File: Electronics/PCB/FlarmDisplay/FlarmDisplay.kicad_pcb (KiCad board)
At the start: 2 copper layers, 43 x 25 mm, 65 parts, among them J1 RJ12, J2 SWD, SW1 RESET, SW2 BOOT, U1 IPN80R3K3P7ATMA1, U2 STM32F334K8Ux, U3 TLC5928, U4 TLC5928, Y1 16MHz

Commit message: Latest
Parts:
- C1, C10, C11, C14, C2, C3, C4, C5, C6, C7, C8, C9, R4, U2, U4, Y1: moved to B.Cu
- J1: footprint Connector_RJ:RJ12_Amphenol_54601 -> FlarmDisplay:RJE231660413T; moved to B.Cu
- U1: footprint Package_TO_SOT_SMD:SOT-323_SC-70 -> Package_TO_SOT_SMD:SOT-223-3_TabPin2; moved to B.Cu
- moved J1 95.1 mm to (101.5, 122.5), turned to 270 degrees
- moved C12 31.3 mm to (95.8, 134.1), turned to 180 degrees
- moved R3 20.1 mm to (88.0, 129.9), turned to 270 degrees
- moved R4 19.8 mm to (82.3, 122.0), turned to 270 degrees
- moved C14 19.7 mm to (81.9, 118.3), turned to 270 degrees
- moved R2 18.5 mm to (120.7, 113.3), turned to 90 degrees
- moved SW2 14.3 mm to (115.1, 113.4), turned to 90 degrees
- moved R1 14.0 mm to (97.7, 118.2), turned to 90 degrees
- moved C7 14.0 mm to (119.9, 123.7), turned to 270 degrees
- moved U4 12.8 mm to (85.9, 117.6)
- moved C6 12.5 mm to (118.9, 123.7)
- moved C11 10.3 mm to (116.7, 130.0)
- moved U1 9.16 mm to (87.5, 130.7), turned to 0 degrees
- moved C9 8.99 mm to (110.9, 115.4), turned to 90 degrees
- moved C10 8.20 mm to (114.1, 130.0), turned to 0 degrees
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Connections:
- net ERR_READ renamed Net-(U4-Pad19)
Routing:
- net +3V3: track 0.00 -> 161.2 mm, vias 0 -> 19
- net GND: track 0.00 -> 128.0 mm, vias 0 -> 15
- net Net-(U2-Pad13): track 0.00 -> 50.0 mm, vias 0 -> 3
- net Net-(U2-Pad12): track 0.00 -> 46.6 mm, vias 0 -> 3
- net Net-(TP3-Pad1): track 0.00 -> 35.8 mm, vias 0 -> 3
- net Net-(D3-Pad1): track 0.00 -> 35.3 mm, vias 0 -> 2
- net Net-(TP4-Pad1): track 0.00 -> 35.0 mm, vias 0 -> 3
- net Net-(U2-Pad14): track 0.00 -> 32.7 mm, vias 0 -> 2
- net Net-(BZ1-Pad2): track 0.00 -> 30.8 mm, vias 0 -> 2
- net NRST: track 0.00 -> 30.0 mm, vias 0 -> 1
- net Net-(D6-Pad1): track 0.00 -> 28.3 mm, vias 0 -> 2
- net Net-(D5-Pad1): track 0.00 -> 26.7 mm, vias 0 -> 2
- net Net-(U2-Pad11): track 0.00 -> 26.3 mm, vias 0 -> 2
- net Net-(U3-Pad19): track 0.00 -> 26.1 mm, vias 0 -> 2
- net SWDAT: track 0.00 -> 25.2 mm, vias 0 -> 2
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- added copper zone on In1.Cu, net +3V3
- added copper zone on In2.Cu, net GND
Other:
- copper layers 2 -> 4

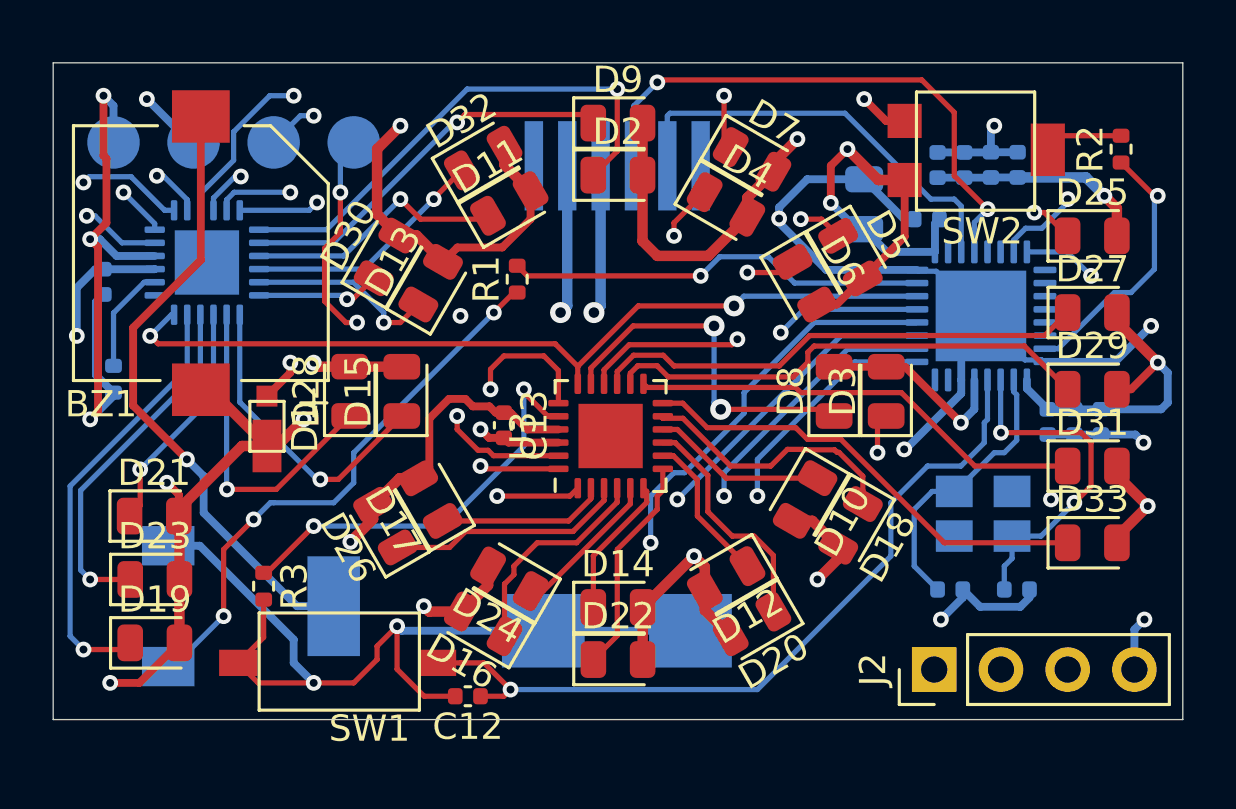
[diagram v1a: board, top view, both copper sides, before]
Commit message: Completed routing, main silk items, 3D models still to go
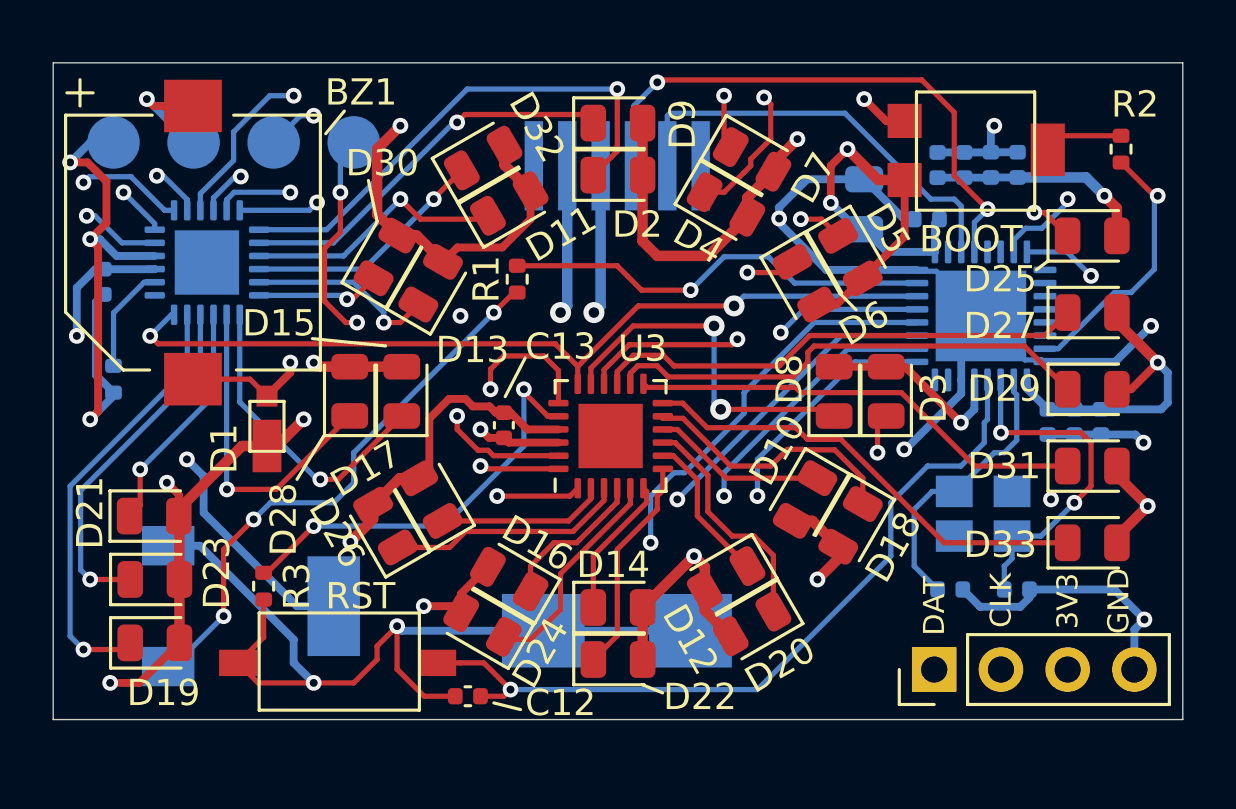
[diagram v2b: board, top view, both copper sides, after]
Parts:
- moved D24 2.02 mm to (96.3, 131.4)
- moved D16 1.97 mm to (97.4, 129.7)
- moved BZ1 0.10 mm to (85.5, 117.0), turned to 0 degrees
- renumbered TP1 to 3V3, TP2 to GND, TP4 to RX, TP3 to TX
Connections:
- J1 pad 1: Net-(J1-Pad1) -> unconnected-(J1-Pad1)
- J1 pad 6: Net-(J1-Pad6) -> unconnected-(J1-Pad6)
- U2 pad 18: Net-(U2-Pad18) -> unconnected-(U2-Pad18)
- U2 pad 21: Net-(U2-Pad21) -> unconnected-(U2-Pad21)
- U2 pad 22: Net-(U2-Pad22) -> unconnected-(U2-Pad22)
- U2 pad 25: Net-(U2-Pad25) -> unconnected-(U2-Pad25)
- U2 pad 26: Net-(U2-Pad26) -> unconnected-(U2-Pad26)
- U2 pad 27: Net-(U2-Pad27) -> unconnected-(U2-Pad27)
- U2 pad 28: Net-(U2-Pad28) -> unconnected-(U2-Pad28)
- U2 pad 29: Net-(U2-Pad29) -> unconnected-(U2-Pad29)
- U2 pad 30: Net-(U2-Pad30) -> unconnected-(U2-Pad30)
- U2 pad 7: Net-(U2-Pad7) -> unconnected-(U2-Pad7)
- U2 pad 8: Net-(U2-Pad8) -> unconnected-(U2-Pad8)
- U4 pad 19: Net-(U4-Pad19) -> unconnected-(U4-Pad19)
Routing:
- net Net-(BZ1-Pad2): track 30.8 -> 18.9 mm
- net Net-(D4-Pad1): track 20.6 -> 30.4 mm
- net Net-(D24-Pad1): track 5.76 -> 8.39 mm
- net Net-(D16-Pad1): track 8.29 -> 5.80 mm
- net GND: track 128.0 -> 129.8 mm, vias 15 -> 14
- net +3V3: track 161.2 -> 159.7 mm
- net Net-(D18-Pad1): track 10.7 -> 10.1 mm
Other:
- net class Default removed
- board text added: "3V3"
- board text added: "BOOT"
- board text added: "CLK"
- board text added: "DAT"
- board text added: "GND"
- board text added: "RST"

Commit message: Completed v1.0
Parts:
- moved BZ1 0.12 mm to (85.4, 117.0)
- moved C11 0.12 mm to (116.6, 130.0)
- moved C12 0.12 mm to (95.7, 134.1)
- moved C13 0.12 mm to (97.0, 123.8)
- moved C14 0.12 mm to (81.8, 118.3)
- moved C3 0.12 mm to (113.5, 113.9)
- moved C4 0.12 mm to (114.6, 113.9)
- moved C5 0.12 mm to (115.6, 113.9)
- moved C6 0.12 mm to (118.8, 123.7)
- moved C7 0.12 mm to (119.8, 123.7)
- moved C8 0.12 mm to (113.1, 116.0)
- moved D1 0.12 mm to (88.1, 123.8)
- moved D12 0.12 mm to (105.5, 129.6)
- moved D13 0.12 mm to (94.3, 118.4)
- moved D14 0.12 mm to (101.4, 130.7)
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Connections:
- U3 pad 25: (no net) -> GND
- U4 pad 25: (no net) -> GND
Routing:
- net GND: vias 14 -> 25

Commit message: Updated PCB to v0.2
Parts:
- removed SW2: BOOT, FlarmDisplay:7814G-1-023E
- added JP1: BOOT, Jumper:SolderJumper-3_P1.3mm_Open_RoundedPad1.0x1.5mm, F.Cu at (112.4, 113.1)
- added U5: MAX318xE, Package_TO_SOT_SMD:SOT-23-5, B.Cu at (119.3, 112.6)
- moved R2 3.65 mm to (121.8, 116.7)
- renumbered 3V3 to TP1, GND to TP2, TX to TP3, RX to TP4
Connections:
- J1 pad 2: TX -> unconnected-(J1-Pad2)
- J1 pad 3: RX -> Net-(J1-Pad3)
- U2 pad 19: TX -> unconnected-(U2-Pad19)
- U3 pad 25: GND -> (no net)
- U4 pad 25: GND -> (no net)
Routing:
- net Net-(J1-Pad3): track 0.00 -> 21.1 mm
- net TX: track 16.3 -> 0.00 mm
- net RX: track 21.4 -> 8.12 mm
- net GND: track 129.8 -> 140.3 mm, vias 25 -> 24
- net Net-(R2-Pad2): track 3.01 -> 12.6 mm, vias 0 -> 2
- net Net-(R2-Pad1): track 10.2 -> 6.27 mm
- net Net-(D4-Pad1): track 30.4 -> 28.5 mm
- net NRST: track 30.0 -> 30.8 mm
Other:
- board text added: "V0.2"

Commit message: Basic firmware LED test working
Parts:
- renumbered TP1 to 3V, TP4 to RX, TP3 to TX
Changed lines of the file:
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@@
     (property "Sheetname" "")
     (attr exclude_from_pos_files)
-    (fp_text reference "TP3" (at -0.254 -1.778) (layer "B.SilkS")
+    (fp_text reference "TX" (at -0.254 -1.778) (layer "B.SilkS")
       (effects (font (size 0.8 0.8) (thickness 0.12)) (justify mirror))
     )
@@
     (property "Sheetname" "")
     (attr exclude_from_pos_files)
-    (fp_text reference "TP4" (at 0 -1.778 180) (layer "B.SilkS")
+    (fp_text reference "RX" (at 0 -1.778 180) (layer "B.SilkS")
       (effects (font (size 0.8 0.8) (thickness 0.12)) (justify mirror))
     )
@@
     (property "Sheetname" "")
     (attr exclude_from_pos_files)
-    (fp_text reference "TP1" (at 0 -1.778) (layer "B.SilkS")
+    (fp_text reference "3V" (at 0 -1.778) (layer "B.SilkS")
       (effects (font (size 0.8 0.8) (thickness 0.12)) (justify mirror))
     )
@@
     (connect_pads (clearance 0.508))
     (min_thickness 0.254) (filled_areas_thickness no)
-    (fill yes (thermal_gap 0.508) (thermal_bridge_width 0.508))
+    (fill (thermal_gap 0.508) (thermal_bridge_width 0.508))
     (polygon
       (pts
@@
     (connect_pads (clearance 0.508))
     (min_thickness 0.254) (filled_areas_thickness no)
-    (fill yes (thermal_gap 0.508) (thermal_bridge_width 0.508))
+    (fill (thermal_gap 0.508) (thermal_bridge_width 0.508))
     (polygon
       (pts
